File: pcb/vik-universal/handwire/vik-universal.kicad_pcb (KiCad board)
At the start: 2 copper layers, 38.5 x 16 mm, 7 parts, among them J1001 Conn_01x01_Socket, J1002 Conn_01x01_Socket

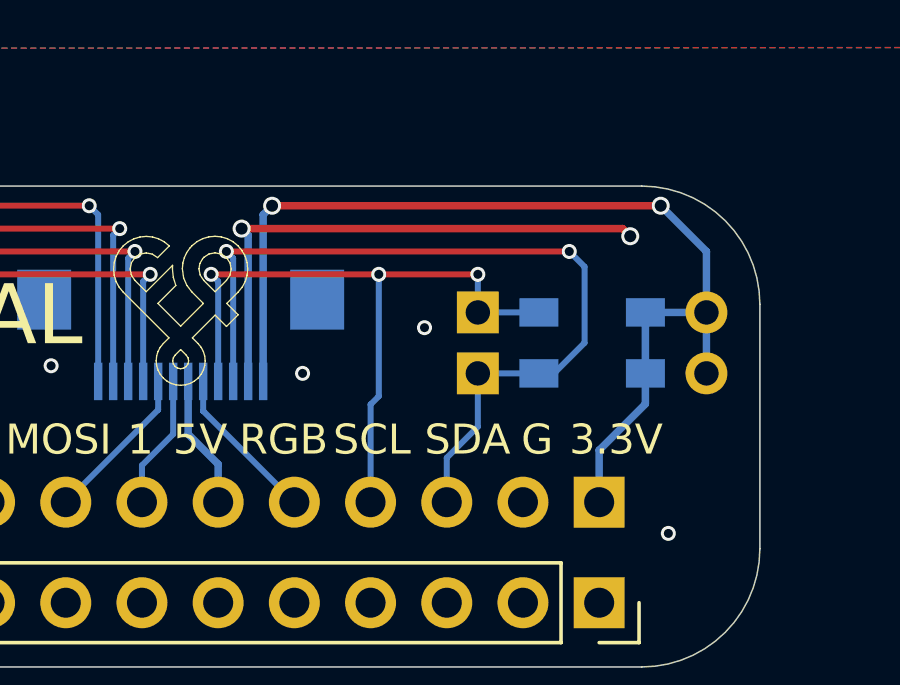
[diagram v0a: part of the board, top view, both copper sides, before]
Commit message: vik universal handwire - added jumpers to enable or disable I2C pull up resistors
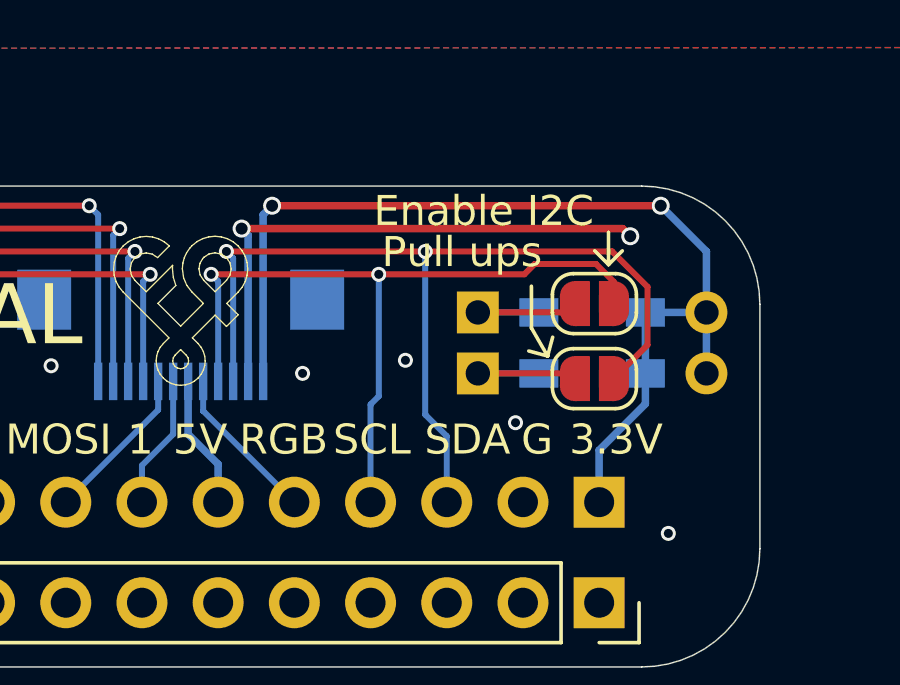
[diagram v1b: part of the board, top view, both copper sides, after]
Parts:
- added JP1001: SolderJumper_2_Open, Jumper:SolderJumper-2_P1.3mm_Open_RoundedPad1.0x1.5mm, F.Cu at (105.1, 90.1)
- added JP1002: SolderJumper_2_Open, Jumper:SolderJumper-2_P1.3mm_Open_RoundedPad1.0x1.5mm, F.Cu at (105.1, 92.6)
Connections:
- R1001 pad 1: SCL -> Net-(JP1001-B)
- R1002 pad 1: SDA -> Net-(JP1002-B)
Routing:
- net Net-(JP1001-B): track 0.00 -> 5.39 mm
- net Net-(JP1002-B): track 0.00 -> 5.34 mm
- net SDA: track 27.8 -> 31.1 mm
- net SCL: track 23.6 -> 25.9 mm, vias 3 -> 2
- net GND: vias 10 -> 11
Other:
- board text added: "Enable I2C"
- board text added: "Pull ups"
